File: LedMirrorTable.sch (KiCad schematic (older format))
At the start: 5 parts

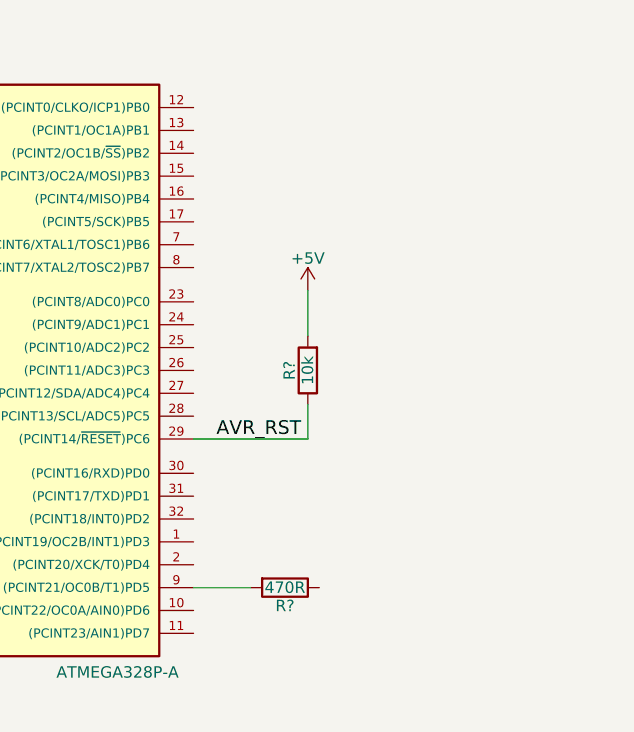
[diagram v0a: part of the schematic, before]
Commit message: Added all components
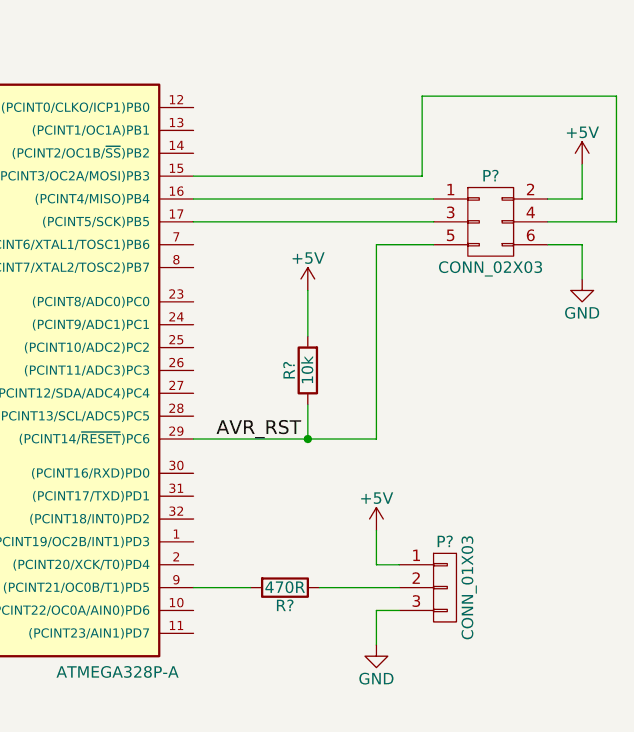
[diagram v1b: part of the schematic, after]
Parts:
- added P?: CONN_01X03, symbol CONN_01X03
- added P?: CONN_02X03, symbol CONN_02X03
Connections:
- net +5V: now also P?.1 (P1), P?.2 (P2)
- net AVR_RST: now also P?.5 (P5)
- net GND: now also P?.3 (P3), P?.6 (P6)
- net at IC?.15 ((PCINT3/OC2A/MOSI)PB3): now also P?.4 (P4)
- net at IC?.16 ((PCINT4/MISO)PB4): now also P?.1 (P1)
- net at IC?.17 ((PCINT5/SCK)PB5): now also P?.3 (P3)
- net at R?.1: now also P?.2 (P2)
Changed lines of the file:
@@
 LIBS:contrib
 LIBS:valves
+LIBS:LedMirrorTable-cache
 EELAYER 25 0
 EELAYER END
@@
 Connection ~ 3600 3600
 Wire Wire Line
-	5800 4450 6300 4450
+	5800 4450 6600 4450
 Wire Wire Line
 	6300 4450 6300 4300
@@
 Wire Wire Line
 	5800 5100 6050 5100
+Wire Wire Line
+	6350 5100 6700 5100
+Wire Wire Line
+	6700 5000 6600 5000
+Wire Wire Line
+	6600 5000 6600 4850
+Wire Wire Line
+	6700 5200 6600 5200
+Wire Wire Line
+	6600 5200 6600 5350
+$Comp
+L +5V #PWR?
+U 1 1 568A76D8
+P 6600 4850
+F 0 "#PWR?" H 6600 4700 50  0001 C CNN
+F 1 "+5V" H 6600 4990 50  0000 C CNN
+F 2 "" H 6600 4850 50  0000 C CNN
+F 3 "" H 6600 4850 50  0000 C CNN
+	1    6600 4850
+	1    0    0    -1
+$EndComp
+$Comp
+L GND #PWR?
+U 1 1 568A76F5
+P 6600 5350
+F 0 "#PWR?" H 6600 5100 50  0001 C CNN
+F 1 "GND" H 6600 5200 50  0000 C CNN
+F 2 "" H 6600 5350 50  0000 C CNN
+F 3 "" H 6600 5350 50  0000 C CNN
+	1    6600 5350
+	1    0    0    -1
+$EndComp
+$Comp
+L CONN_01X03 P?
+U 1 1 568A779C
+P 6900 5100
+F 0 "P?" H 6900 5300 50  0000 C CNN
+F 1 "CONN_01X03" V 7000 5100 50  0000 C CNN
+F 2 "" H 6900 5100 50  0000 C CNN
+F 3 "" H 6900 5100 50  0000 C CNN
+	1    6900 5100
+	1    0    0    -1
+$EndComp
+$Comp
+L CONN_02X03 P?
+U 1 1 568A78C3
+P 7100 3500
+F 0 "P?" H 7100 3700 50  0000 C CNN
+F 1 "CONN_02X03" H 7100 3300 50  0000 C CNN
+F 2 "" H 7100 2300 50  0000 C CNN
+F 3 "" H 7100 2300 50  0000 C CNN
+	1    7100 3500
+	1    0    0    -1
+$EndComp
+Wire Wire Line
+	5800 3400 6850 3400
+Wire Wire Line
+	5800 3500 6850 3500
+Wire Wire Line
+	6600 4450 6600 3600
+Wire Wire Line
+	6600 3600 6850 3600
+Connection ~ 6300 4450
+$Comp
+L +5V #PWR?
+U 1 1 568A79BD
+P 7500 3250
+F 0 "#PWR?" H 7500 3100 50  0001 C CNN
+F 1 "+5V" H 7500 3390 50  0000 C CNN
+F 2 "" H 7500 3250 50  0000 C CNN
+F 3 "" H 7500 3250 50  0000 C CNN
+	1    7500 3250
+	1    0    0    -1
+$EndComp
+Wire Wire Line
+	7350 3400 7500 3400
+Wire Wire Line
+	7500 3400 7500 3250
+Wire Wire Line
+	7350 3600 7500 3600
+Wire Wire Line
+	7500 3600 7500 3750
+$Comp
+L GND #PWR?
+U 1 1 568A7A36
+P 7500 3750
+F 0 "#PWR?" H 7500 3500 50  0001 C CNN
+F 1 "GND" H 7500 3600 50  0000 C CNN
+F 2 "" H 7500 3750 50  0000 C CNN
+F 3 "" H 7500 3750 50  0000 C CNN
+	1    7500 3750
+	1    0    0    -1
+$EndComp
+Wire Wire Line
+	5800 3300 6800 3300
+Wire Wire Line
+	6800 3300 6800 2950
+Wire Wire Line
+	6800 2950 7650 2950
+Wire Wire Line
+	7650 2950 7650 3500
+Wire Wire Line
+	7650 3500 7350 3500
 $EndSCHEMATC

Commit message: Added labels
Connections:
- net PROG_MOSI: now reaches IC?.15 ((PCINT3/OC2A/MOSI)PB3), P?.4 (P4)
- net PROG_MISO: now reaches IC?.16 ((PCINT4/MISO)PB4), P?.1 (P1)
- net PROG_SCK: now reaches IC?.17 ((PCINT5/SCK)PB5), P?.3 (P3)
- net D_OUT: now reaches IC?.9 ((PCINT21/OC0B/T1)PD5), R?.2
- net D_STRIP: now reaches P?.2 (P2), R?.1
- net AVR_RST renamed RESET
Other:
- note added: "Programming\nHeader"
- note added: "To NeoPixel Strip"
- moved on the sheet: P?, R?
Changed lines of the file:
@@
 encoding utf-8
 Sheet 1 1
-Title ""
+Title "NeoPixel Strip Driver"
 Date ""
 Rev ""
@@
 $EndComp
 Wire Wire Line
-	3000 3000 3900 3000
+	3000 3000 3150 3000
+Wire Wire Line
+	3150 3000 3600 3000
+Wire Wire Line
+	3600 3000 3900 3000
 Wire Wire Line
 	6300 3800 6300 4000
 Connection ~ 3150 3000
 Wire Wire Line
-	3600 3000 3600 4650
+	3600 3000 3600 3100
+Wire Wire Line
+	3600 3100 3600 3300
+Wire Wire Line
+	3600 3300 3600 3600
+Wire Wire Line
+	3600 3600 3600 4650
 Wire Wire Line
 	3600 3100 3900 3100
@@
 Connection ~ 3600 3300
 Wire Wire Line
-	3600 4950 3600 5450
+	3600 4950 3600 5100
+Wire Wire Line
+	3600 5100 3600 5200
+Wire Wire Line
+	3600 5200 3600 5300
+Wire Wire Line
+	3600 5300 3600 5450
 Wire Wire Line
 	3600 5100 3900 5100
@@
 Connection ~ 3600 3600
 Wire Wire Line
-	5800 4450 6600 4450
+	5800 4450 6300 4450
+Wire Wire Line
+	6300 4450 6600 4450
 Wire Wire Line
 	6300 4450 6300 4300
@@
 Wire Wire Line
 	3150 2800 3150 3000
-Text Label 5900 4450 0    60   ~ 0
-AVR_RST
+Text Label 5850 4450 0    60   ~ 0
+RESET
 Wire Wire Line
 	3000 3200 3150 3200
@@
 L R R?
 U 1 1 568A747E
-P 6200 5100
-F 0 "R?" V 6280 5100 50  0000 C CNN
-F 1 "470R" V 6200 5100 50  0000 C CNN
-F 2 "" V 6130 5100 50  0000 C CNN
-F 3 "" H 6200 5100 50  0000 C CNN
-	1    6200 5100
+P 6350 5100
+F 0 "R?" V 6430 5100 50  0000 C CNN
+F 1 "470R" V 6350 5100 50  0000 C CNN
+F 2 "" V 6280 5100 50  0000 C CNN
+F 3 "" H 6350 5100 50  0000 C CNN
+	1    6350 5100
 	0    1    1    0
 $EndComp
 Wire Wire Line
-	5800 5100 6050 5100
-Wire Wire Line
-	6350 5100 6700 5100
-Wire Wire Line
-	6700 5000 6600 5000
-Wire Wire Line
-	6600 5000 6600 4850
-Wire Wire Line
-	6700 5200 6600 5200
-Wire Wire Line
-	6600 5200 6600 5350
+	5800 5100 6200 5100
+Wire Wire Line
+	6500 5100 7100 5100
+Wire Wire Line
+	7100 5000 6950 5000
+Wire Wire Line
+	6950 5000 6950 4850
+Wire Wire Line
+	7100 5200 6950 5200
+Wire Wire Line
+	6950 5200 6950 5350
 $Comp
 L +5V #PWR?
 U 1 1 568A76D8
-P 6600 4850
-F 0 "#PWR?" H 6600 4700 50  0001 C CNN
-F 1 "+5V" H 6600 4990 50  0000 C CNN
-F 2 "" H 6600 4850 50  0000 C CNN
-F 3 "" H 6600 4850 50  0000 C CNN
-	1    6600 4850
+P 6950 4850
+F 0 "#PWR?" H 6950 4700 50  0001 C CNN
+F 1 "+5V" H 6950 4990 50  0000 C CNN
+F 2 "" H 6950 4850 50  0000 C CNN
+F 3 "" H 6950 4850 50  0000 C CNN
+	1    6950 4850
 	1    0    0    -1
 $EndComp
@@
 L GND #PWR?
 U 1 1 568A76F5
-P 6600 5350
-F 0 "#PWR?" H 6600 5100 50  0001 C CNN
-F 1 "GND" H 6600 5200 50  0000 C CNN
-F 2 "" H 6600 5350 50  0000 C CNN
-F 3 "" H 6600 5350 50  0000 C CNN
-	1    6600 5350
+P 6950 5350
+F 0 "#PWR?" H 6950 5100 50  0001 C CNN
+F 1 "GND" H 6950 5200 50  0000 C CNN
+F 2 "" H 6950 5350 50  0000 C CNN
+F 3 "" H 6950 5350 50  0000 C CNN
+	1    6950 5350
 	1    0    0    -1
 $EndComp
@@
 L CONN_01X03 P?
 U 1 1 568A779C
-P 6900 5100
-F 0 "P?" H 6900 5300 50  0000 C CNN
-F 1 "CONN_01X03" V 7000 5100 50  0000 C CNN
-F 2 "" H 6900 5100 50  0000 C CNN
-F 3 "" H 6900 5100 50  0000 C CNN
-	1    6900 5100
+P 7300 5100
+F 0 "P?" H 7300 5300 50  0000 C CNN
+F 1 "CONN_01X03" V 7400 5100 50  0000 C CNN
+F 2 "" H 7300 5100 50  0000 C CNN
+F 3 "" H 7300 5100 50  0000 C CNN
+	1    7300 5100
 	1    0    0    -1
 $EndComp
@@
 Wire Wire Line
 	7650 3500 7350 3500
+Text Label 5850 5100 0    60   ~ 0
+D_OUT
+Text Label 6550 5100 0    60   ~ 0
+D_STRIP
+Text Label 5850 3300 0    60   ~ 0
+PROG_MOSI
+Text Label 5850 3400 0    60   ~ 0
+PROG_MISO
+Text Label 5850 3500 0    60   ~ 0
+PROG_SCK
+Text Notes 6750 3950 0    60   ~ 0
+Programming\nHeader
+Text Notes 7650 5500 1    60   ~ 0
+To NeoPixel Strip
 $EndSCHEMATC

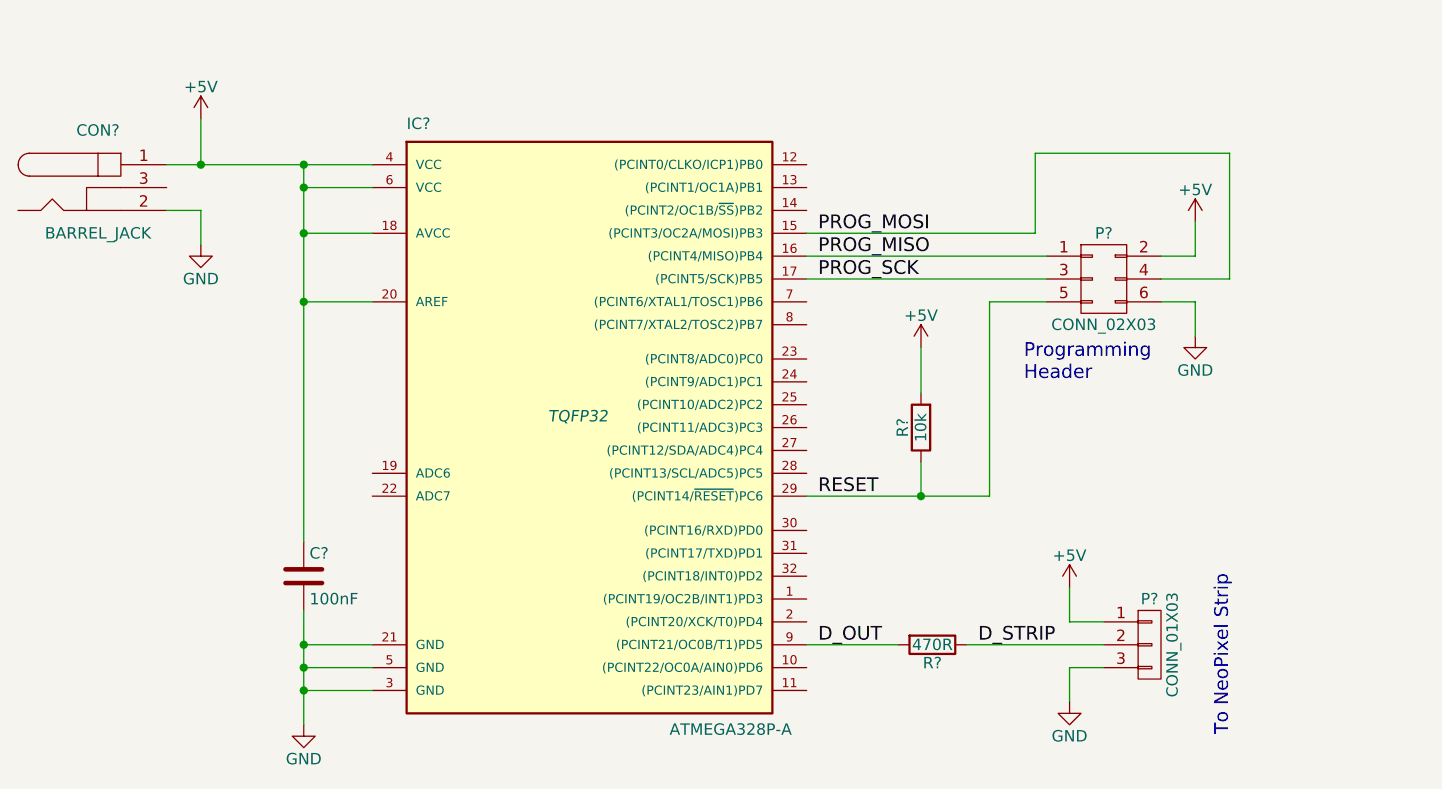
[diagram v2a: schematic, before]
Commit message: Removed unused libraries. Changed JST connector to 3-pin header
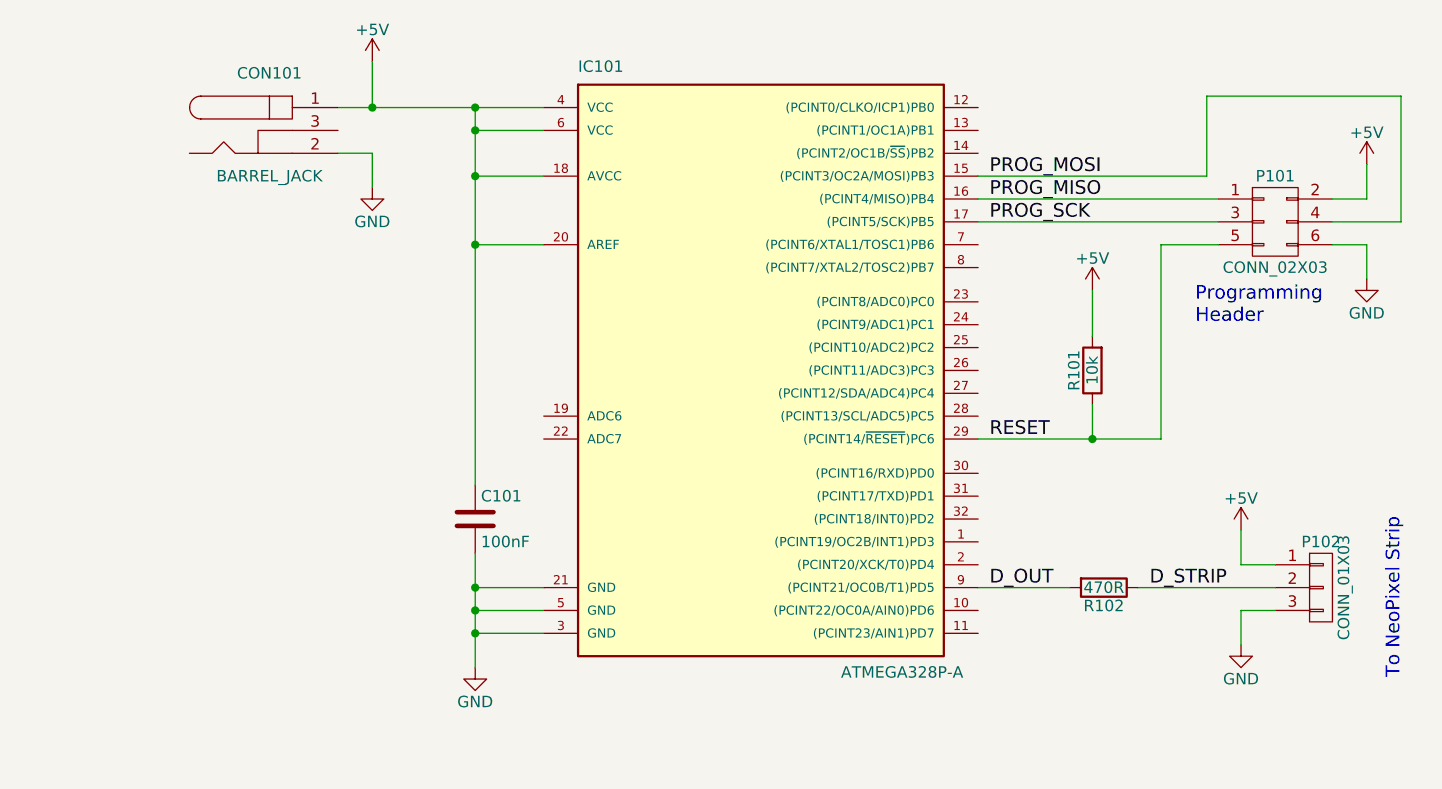
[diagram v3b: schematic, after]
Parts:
- C101: renamed from C?; footprint (none) -> Capacitors_SMD:C_0603_HandSoldering
- CON101: renamed from CON?; footprint (none) -> Connect:JACK_ALIM
- IC101: renamed from IC?; footprint TQFP32 -> Housings_QFP:TQFP-32_7x7mm_Pitch0.8mm
- P101: renamed from P?; footprint (none) -> Pin_Headers:Pin_Header_Straight_2x03
- P102: renamed from P?; footprint (none) -> Pin_Headers:Pin_Header_Straight_1x03
- R101, R102: renamed from R?; footprint (none) -> Resistors_SMD:R_0603_HandSoldering
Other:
- moved on the sheet: C101, CON101, IC101, P101, P102, R101, R102

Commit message: Created PCB
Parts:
- removed CON101: BARREL_JACK, Connect:JACK_ALIM, symbol BARREL_JACK
- removed P101: CONN_02X03, Pin_Headers:Pin_Header_Straight_2x03, symbol CONN_02X03
- added J101: POWER_JACKSMD, SparkFun-Connectors:SparkFun-Connectors-POWER_JACK_SMD, symbol POWER_JACKSMD
- added JP101: M03X2, SparkFun-Connectors:SparkFun-Connectors-2X3_SMD, symbol M03X2
- renumbered P102 to P101
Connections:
- net +5V: now also J101.VIN0 (PWR), J101.VIN1 (PWR), JP101.2
- net GND: now also J101.GND, JP101.6
- net PROG_MISO: now also JP101.1
- net PROG_MOSI: now also JP101.4
- net PROG_SCK: now also JP101.3
- net RESET: now also JP101.5
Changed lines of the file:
@@
 LIBS:contrib
 LIBS:valves
+LIBS:SparkFun-Connectors
 LIBS:LedMirrorTable-cache
 EELAYER 25 0
@@
 $EndComp
 $Comp
-L BARREL_JACK CON101
-U 1 1 568A6DBE
-P 3450 2850
-F 0 "CON101" H 3450 3100 50  0000 C CNN
-F 1 "BARREL_JACK" H 3450 2650 50  0000 C CNN
-F 2 "Connect:JACK_ALIM" H 3450 2850 50  0001 C CNN
-F 3 "" H 3450 2850 50  0000 C CNN
-	1    3450 2850
-	1    0    0    -1
-$EndComp
-$Comp
 L C C101
 U 1 1 568A6E6B
@@
 $EndComp
 $Comp
-L CONN_01X03 P102
+L CONN_01X03 P101
 U 1 1 568A779C
 P 8050 4850
-F 0 "P102" H 8050 5050 50  0000 C CNN
+F 0 "P101" H 8050 5050 50  0000 C CNN
 F 1 "CONN_01X03" V 8150 4850 50  0000 C CNN
 F 2 "Pin_Headers:Pin_Header_Straight_1x03" H 8050 4850 50  0001 C CNN
@@
 	1    0    0    -1
 $EndComp
-$Comp
-L CONN_02X03 P101
-U 1 1 568A78C3
-P 7850 3250
-F 0 "P101" H 7850 3450 50  0000 C CNN
-F 1 "CONN_02X03" H 7850 3050 50  0000 C CNN
-F 2 "Pin_Headers:Pin_Header_Straight_2x03" H 7850 2050 50  0001 C CNN
-F 3 "" H 7850 2050 50  0000 C CNN
-	1    7850 3250
-	1    0    0    -1
-$EndComp
 Wire Wire Line
 	6550 3150 7600 3150
@@
 L +5V #PWR07
 U 1 1 568A79BD
-P 8250 3000
-F 0 "#PWR07" H 8250 2850 50  0001 C CNN
-F 1 "+5V" H 8250 3140 50  0000 C CNN
-F 2 "" H 8250 3000 50  0000 C CNN
-F 3 "" H 8250 3000 50  0000 C CNN
-	1    8250 3000
-	1    0    0    -1
-$EndComp
-Wire Wire Line
-	8100 3150 8250 3150
-Wire Wire Line
-	8250 3150 8250 3000
-Wire Wire Line
-	8100 3350 8250 3350
-Wire Wire Line
-	8250 3350 8250 3500
+P 8350 3000
+F 0 "#PWR07" H 8350 2850 50  0001 C CNN
+F 1 "+5V" H 8350 3140 50  0000 C CNN
+F 2 "" H 8350 3000 50  0000 C CNN
+F 3 "" H 8350 3000 50  0000 C CNN
+	1    8350 3000
+	1    0    0    -1
+$EndComp
+Wire Wire Line
+	8200 3150 8350 3150
+Wire Wire Line
+	8350 3150 8350 3000
+Wire Wire Line
+	8200 3350 8350 3350
+Wire Wire Line
+	8350 3350 8350 3500
 $Comp
 L GND #PWR08
 U 1 1 568A7A36
-P 8250 3500
-F 0 "#PWR08" H 8250 3250 50  0001 C CNN
-F 1 "GND" H 8250 3350 50  0000 C CNN
-F 2 "" H 8250 3500 50  0000 C CNN
-F 3 "" H 8250 3500 50  0000 C CNN
-	1    8250 3500
+P 8350 3500
+F 0 "#PWR08" H 8350 3250 50  0001 C CNN
+F 1 "GND" H 8350 3350 50  0000 C CNN
+F 2 "" H 8350 3500 50  0000 C CNN
+F 3 "" H 8350 3500 50  0000 C CNN
+	1    8350 3500
 	1    0    0    -1
 $EndComp
@@
 	7550 3050 7550 2700
 Wire Wire Line
-	7550 2700 8400 2700
-Wire Wire Line
-	8400 2700 8400 3250
-Wire Wire Line
-	8400 3250 8100 3250
+	7550 2700 8500 2700
+Wire Wire Line
+	8500 2700 8500 3250
+Wire Wire Line
+	8500 3250 8200 3250
 Text Label 6600 4850 0    60   ~ 0
 D_OUT
@@
 Text Label 6600 3250 0    60   ~ 0
 PROG_SCK
-Text Notes 7500 3700 0    60   ~ 0
+Text Notes 7600 3750 0    60   ~ 0
 Programming\nHeader
 Text Notes 8400 5250 1    60   ~ 0
 To NeoPixel Strip
+$Comp
+L M03X2 JP101
+U 1 1 568A8DB0
+P 7900 3250
+F 0 "JP101" H 7700 3470 50  0000 L BNN
+F 1 "M03X2" H 7700 2970 50  0000 L BNN
+F 2 "SparkFun-Connectors:SparkFun-Connectors-2X3_SMD" H 7930 3400 20  0001 C CNN
+F 3 "" H 7900 3250 60  0000 C CNN
+	1    7900 3250
+	1    0    0    -1
+$EndComp
+$Comp
+L POWER_JACKSMD J101
+U 1 1 568A8DED
+P 3650 3050
+F 0 "J101" H 3250 3050 50  0000 L BNN
+F 1 "POWER_JACKSMD" H 3250 3450 50  0000 L BNN
+F 2 "SparkFun-Connectors:SparkFun-Connectors-POWER_JACK_SMD" H 3680 3200 20  0001 C CNN
+F 3 "" H 3650 3050 60  0000 C CNN
+	1    3650 3050
+	1    0    0    -1
+$EndComp
 $EndSCHEMATC
